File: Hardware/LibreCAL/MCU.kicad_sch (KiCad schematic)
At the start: 30 parts, among them J5 USB_C_Receptacle_USB2.0, J6 TC2030-ARM, SW1 TL3301CF160QG, U5 W25Q16JVSNIQ, U6 IP4234CZ6, U7 RP2040, U8 W25Q16JVSNIQ, Y1 ECS-120-8-36-CKM-TR3

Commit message: Partial routing
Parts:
- removed Y1: ECS-120-8-36-CKM-TR3, Crystal:Crystal_SMD_2520-4Pin_2.5x2.0mm, symbol Device:Crystal_GND2
- added Y1: ECS-120-8-36-CKM-TR3, Crystal:Crystal_SMD_2520-4Pin_2.5x2.0mm, symbol Device:Crystal_GND24
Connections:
- net ADC_TEMP: now also U7.41 (GPIO29_ADC3); no longer U7.38 (GPIO26_ADC0)
- net BUTTON1: now also U7.6 (GPIO4); no longer U7.40 (GPIO28_ADC2)
- net GND: now also Y1.2, Y1.4
- net HEATER: now also U7.40 (GPIO28_ADC2); no longer U7.41 (GPIO29_ADC3)
- net LED_LOAD: now also U7.37 (GPIO25); no longer U7.31 (GPIO20)
- net LED_OPEN: now also U7.35 (GPIO23); no longer U7.29 (GPIO18)
- net LED_PORT1: now also U7.32 (GPIO21); no longer U7.34 (GPIO22)
- net LED_PORT2: now also U7.9 (GPIO7); no longer U7.35 (GPIO23)
- net LED_PORT3: now also U7.34 (GPIO22); no longer U7.36 (GPIO24)
- net LED_PORT4: now also U7.11 (GPIO8); no longer U7.37 (GPIO25)
- net LED_READY: now also U7.7 (GPIO5); no longer U7.27 (GPIO16)
- net LED_SHORT: now also U7.36 (GPIO24); no longer U7.30 (GPIO19)
- net LED_THROUGH: now also U7.38 (GPIO26_ADC0); no longer U7.32 (GPIO21)
- net LED_WAIT: now also U7.8 (GPIO6); no longer U7.28 (GPIO17)
- net P1_V1: now also U7.29 (GPIO18); no longer U7.6 (GPIO4)
- net P1_V2: now also U7.30 (GPIO19); no longer U7.7 (GPIO5)
- net P1_V3: now also U7.31 (GPIO20); no longer U7.8 (GPIO6)
- net P2_V1: now also U7.28 (GPIO17); no longer U7.9 (GPIO7)
- net P2_V2: now also U7.27 (GPIO16); no longer U7.11 (GPIO8)
- net P2_V3: now also U7.18 (GPIO15); no longer U7.12 (GPIO9)
- net P3_V1: now also U7.14 (GPIO11); no longer U7.13 (GPIO10)
- net P3_V2: now also U7.13 (GPIO10); no longer U7.14 (GPIO11)
- net P3_V3: now also U7.12 (GPIO9); no longer U7.15 (GPIO12)
- net P4_V1: now also U7.15 (GPIO12); no longer U7.16 (GPIO13)
- net P4_V2: now also U7.16 (GPIO13); no longer U7.17 (GPIO14)
- net P4_V3: now also U7.17 (GPIO14); no longer U7.18 (GPIO15)
- net at C12.1, U7.20 (XIN): now also Y1.1
- net at J5.A7 (D-), J5.B7 (D-): now also U6.6 (I/O2A); no longer U6.1 (I/O1A)
- net at U6.3 (I/O1B): now also U7.47 (USB_DP); no longer U7.46 (USB_DM)
- net at U6.4 (I/O2B): now also U7.46 (USB_DM); no longer U7.47 (USB_DP)
- net at J5.A6 (D+), J5.B6 (D+): now also U6.1 (I/O1A); no longer U6.6 (I/O2A)
- net at C13.1, U7.21 (XOUT): now also Y1.3
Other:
- moved on the sheet: U6

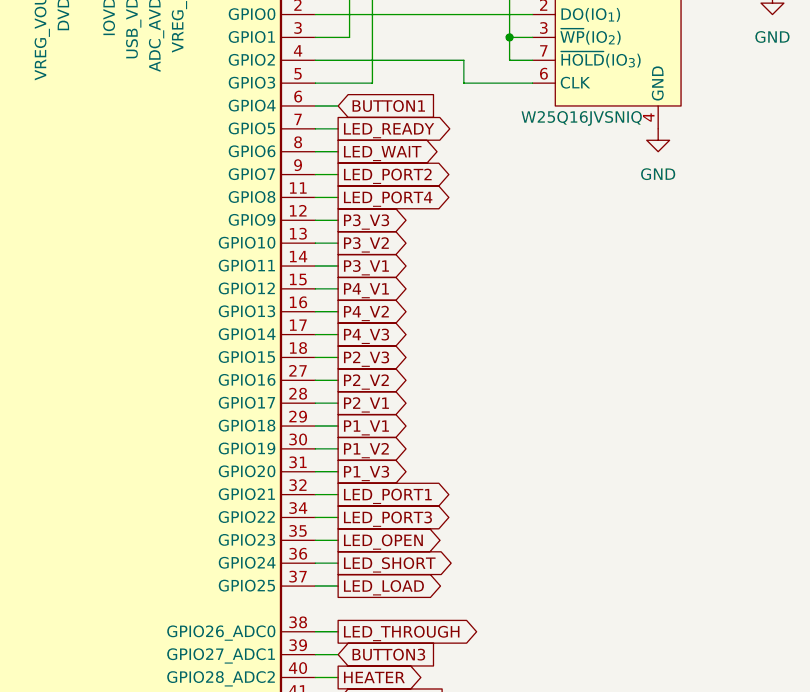
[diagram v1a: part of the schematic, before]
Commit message: Filters added, housing updated
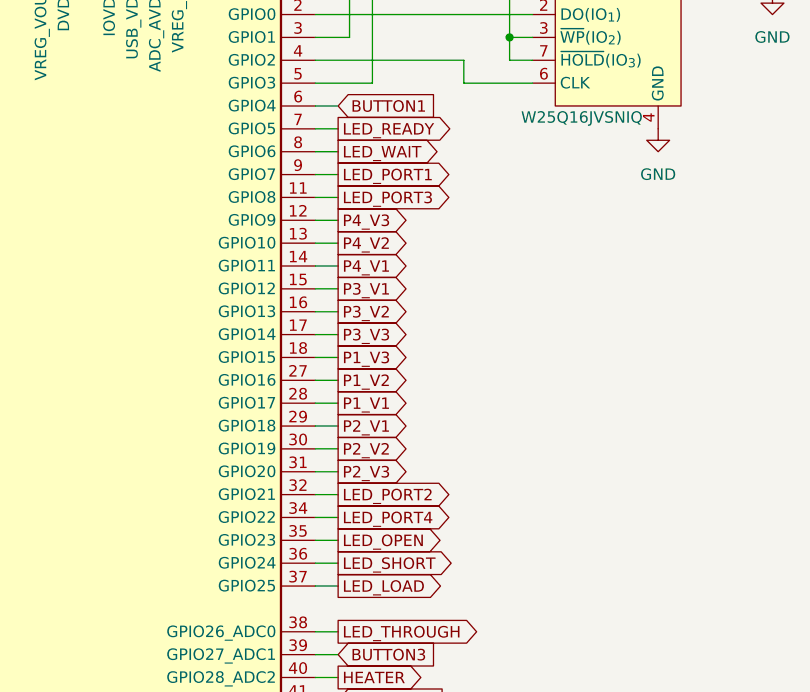
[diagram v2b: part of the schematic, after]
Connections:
- net LED_PORT1: now also U7.9 (GPIO7); no longer U7.32 (GPIO21)
- net LED_PORT2: now also U7.32 (GPIO21); no longer U7.9 (GPIO7)
- net LED_PORT3: now also U7.11 (GPIO8); no longer U7.34 (GPIO22)
- net LED_PORT4: now also U7.34 (GPIO22); no longer U7.11 (GPIO8)
- net P1_V1: now also U7.28 (GPIO17); no longer U7.29 (GPIO18)
- net P1_V2: now also U7.27 (GPIO16); no longer U7.30 (GPIO19)
- net P1_V3: now also U7.18 (GPIO15); no longer U7.31 (GPIO20)
- net P2_V1: now also U7.29 (GPIO18); no longer U7.28 (GPIO17)
- net P2_V2: now also U7.30 (GPIO19); no longer U7.27 (GPIO16)
- net P2_V3: now also U7.31 (GPIO20); no longer U7.18 (GPIO15)
- net P3_V1: now also U7.15 (GPIO12); no longer U7.14 (GPIO11)
- net P3_V2: now also U7.16 (GPIO13); no longer U7.13 (GPIO10)
- net P3_V3: now also U7.17 (GPIO14); no longer U7.12 (GPIO9)
- net P4_V1: now also U7.14 (GPIO11); no longer U7.15 (GPIO12)
- net P4_V2: now also U7.13 (GPIO10); no longer U7.16 (GPIO13)
- net P4_V3: now also U7.12 (GPIO9); no longer U7.17 (GPIO14)
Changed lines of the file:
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@@
     )
   )
-  (global_label "P4_V3" (shape output) (at 204.47 107.95 0) (fields_autoplaced)
+  (global_label "P3_V3" (shape output) (at 204.47 107.95 0) (fields_autoplaced)
     (effects (font (size 1.27 1.27)) (justify left))
     (property "Intersheet References" "${INTERSHEET_REFS}" (id 0) (at 212.6283 107.8706 0)
@@
     )
   )
-  (global_label "P3_V1" (shape output) (at 204.47 100.33 0) (fields_autoplaced)
+  (global_label "P4_V1" (shape output) (at 204.47 100.33 0) (fields_autoplaced)
     (effects (font (size 1.27 1.27)) (justify left))
     (property "Intersheet References" "${INTERSHEET_REFS}" (id 0) (at 212.6283 100.2506 0)
@@
     )
   )
-  (global_label "P1_V3" (shape output) (at 204.47 123.19 0) (fields_autoplaced)
+  (global_label "P2_V3" (shape output) (at 204.47 123.19 0) (fields_autoplaced)
     (effects (font (size 1.27 1.27)) (justify left))
     (property "Intersheet References" "${INTERSHEET_REFS}" (id 0) (at 212.6283 123.1106 0)
@@
     )
   )
-  (global_label "LED_PORT4" (shape output) (at 204.47 92.71 0) (fields_autoplaced)
+  (global_label "LED_PORT3" (shape output) (at 204.47 92.71 0) (fields_autoplaced)
     (effects (font (size 1.27 1.27)) (justify left))
     (property "Intersheet References" "${INTERSHEET_REFS}" (id 0) (at 217.3455 92.6306 0)
@@
     )
   )
-  (global_label "P1_V1" (shape output) (at 204.47 118.11 0) (fields_autoplaced)
+  (global_label "P2_V1" (shape output) (at 204.47 118.11 0) (fields_autoplaced)
     (effects (font (size 1.27 1.27)) (justify left))
     (property "Intersheet References" "${INTERSHEET_REFS}" (id 0) (at 212.6283 118.0306 0)
@@
     )
   )
-  (global_label "P3_V2" (shape output) (at 204.47 97.79 0) (fields_autoplaced)
+  (global_label "P4_V2" (shape output) (at 204.47 97.79 0) (fields_autoplaced)
     (effects (font (size 1.27 1.27)) (justify left))
     (property "Intersheet References" "${INTERSHEET_REFS}" (id 0) (at 212.6283 97.7106 0)
@@
     )
   )
-  (global_label "LED_PORT1" (shape output) (at 204.47 125.73 0) (fields_autoplaced)
+  (global_label "LED_PORT2" (shape output) (at 204.47 125.73 0) (fields_autoplaced)
     (effects (font (size 1.27 1.27)) (justify left))
     (property "Intersheet References" "${INTERSHEET_REFS}" (id 0) (at 217.3455 125.6506 0)
@@
     )
   )
-  (global_label "P2_V1" (shape output) (at 204.47 115.57 0) (fields_autoplaced)
+  (global_label "P1_V1" (shape output) (at 204.47 115.57 0) (fields_autoplaced)
     (effects (font (size 1.27 1.27)) (justify left))
     (property "Intersheet References" "${INTERSHEET_REFS}" (id 0) (at 212.6283 115.4906 0)
@@
     )
   )
-  (global_label "P2_V2" (shape output) (at 204.47 113.03 0) (fields_autoplaced)
+  (global_label "P1_V2" (shape output) (at 204.47 113.03 0) (fields_autoplaced)
     (effects (font (size 1.27 1.27)) (justify left))
     (property "Intersheet References" "${INTERSHEET_REFS}" (id 0) (at 212.6283 112.9506 0)
@@
     )
   )
-  (global_label "P4_V2" (shape output) (at 204.47 105.41 0) (fields_autoplaced)
+  (global_label "P3_V2" (shape output) (at 204.47 105.41 0) (fields_autoplaced)
     (effects (font (size 1.27 1.27)) (justify left))
     (property "Intersheet References" "${INTERSHEET_REFS}" (id 0) (at 212.6283 105.3306 0)
@@
     )
   )
-  (global_label "P4_V1" (shape output) (at 204.47 102.87 0) (fields_autoplaced)
+  (global_label "P3_V1" (shape output) (at 204.47 102.87 0) (fields_autoplaced)
     (effects (font (size 1.27 1.27)) (justify left))
     (property "Intersheet References" "${INTERSHEET_REFS}" (id 0) (at 212.6283 102.7906 0)
@@
     )
   )
-  (global_label "LED_PORT3" (shape output) (at 204.47 128.27 0) (fields_autoplaced)
+  (global_label "LED_PORT4" (shape output) (at 204.47 128.27 0) (fields_autoplaced)
     (effects (font (size 1.27 1.27)) (justify left))
     (property "Intersheet References" "${INTERSHEET_REFS}" (id 0) (at 217.3455 128.1906 0)
@@
     )
   )
-  (global_label "P2_V3" (shape output) (at 204.47 110.49 0) (fields_autoplaced)
+  (global_label "P1_V3" (shape output) (at 204.47 110.49 0) (fields_autoplaced)
     (effects (font (size 1.27 1.27)) (justify left))
     (property "Intersheet References" "${INTERSHEET_REFS}" (id 0) (at 212.6283 110.4106 0)
@@
     )
   )
-  (global_label "P3_V3" (shape output) (at 204.47 95.25 0) (fields_autoplaced)
+  (global_label "P4_V3" (shape output) (at 204.47 95.25 0) (fields_autoplaced)
     (effects (font (size 1.27 1.27)) (justify left))
     (property "Intersheet References" "${INTERSHEET_REFS}" (id 0) (at 212.6283 95.1706 0)
@@
     )
   )
-  (global_label "LED_PORT2" (shape output) (at 204.47 90.17 0) (fields_autoplaced)
+  (global_label "LED_PORT1" (shape output) (at 204.47 90.17 0) (fields_autoplaced)
     (effects (font (size 1.27 1.27)) (justify left))
     (property "Intersheet References" "${INTERSHEET_REFS}" (id 0) (at 217.3455 90.0906 0)
@@
     )
   )
-  (global_label "P1_V2" (shape output) (at 204.47 120.65 0) (fields_autoplaced)
+  (global_label "P2_V2" (shape output) (at 204.47 120.65 0) (fields_autoplaced)
     (effects (font (size 1.27 1.27)) (justify left))
     (property "Intersheet References" "${INTERSHEET_REFS}" (id 0) (at 212.6283 120.5706 0)

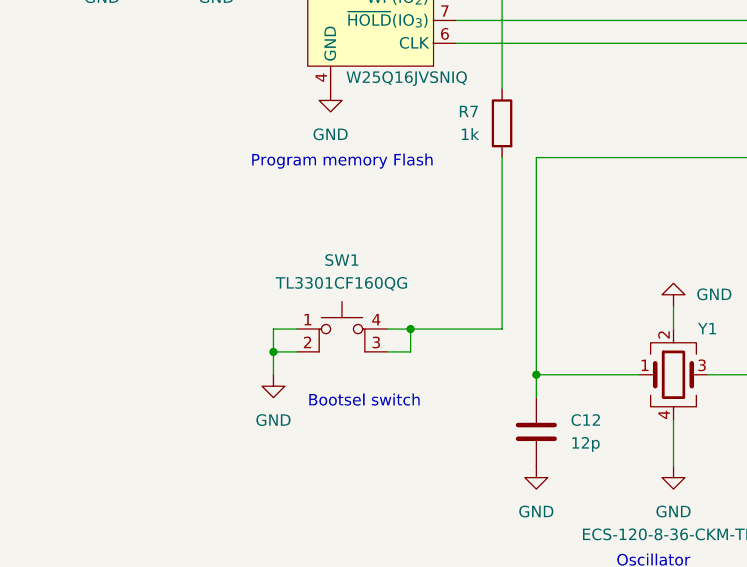
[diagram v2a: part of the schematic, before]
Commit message: replaced bootsel switch, adjusted covers
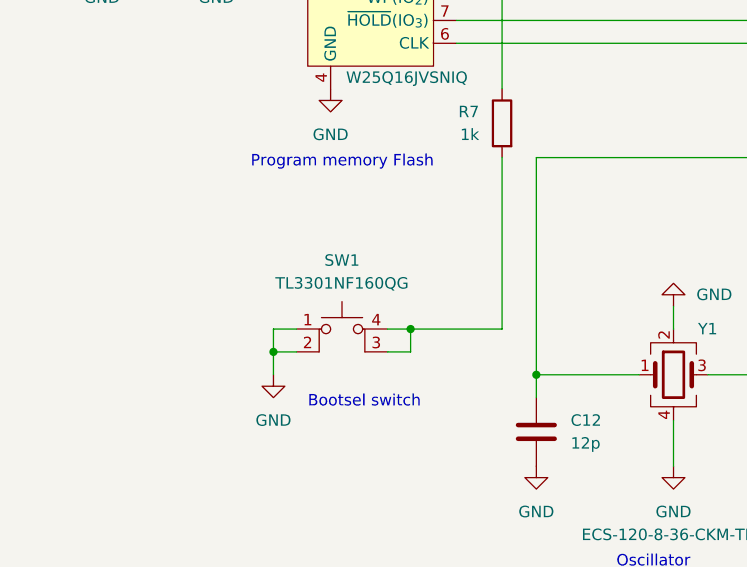
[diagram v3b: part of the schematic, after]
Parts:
- SW1: value TL3301CF160QG -> TL3301NF160QG; footprint LibreCAL:TL3301-J -> LibreCAL:TL3301N-J
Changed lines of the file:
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@@
     (in_bom yes) (on_board yes) (fields_autoplaced)
     (property "Reference" "SW1" (id 0) (at 57.15 129.54 0))
-    (property "Value" "TL3301CF160QG" (id 1) (at 57.15 132.08 0))
-    (property "Footprint" "LibreCAL:TL3301-J" (id 2) (at 57.15 132.08 0)
+    (property "Value" "TL3301NF160QG" (id 1) (at 57.15 132.08 0))
+    (property "Footprint" "LibreCAL:TL3301N-J" (id 2) (at 57.15 132.08 0)
       (effects (font (size 1.27 1.27)) hide)
     )

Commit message: Improvements on LibreCAL KiCad: fixed minor errors/labels(cosmetic), improved BOM(Added LCSC_Part), improved Impedance JLCPCB 4Layer JLC7628 1.6mm
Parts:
- C10, C21, C23, C24, C25: LCSC_Part (none) -> C307418
- C11, C14, C15, C16, C17, C18, C19, C20, C22, C26, C9: LCSC_Part (none) -> C307331
- C12, C13: LCSC_Part (none) -> C76948
- FB1: LCSC_Part (none) -> C404693
- J5: LCSC_Part (none) -> C165948
- J6: LCSC_Part (none) -> NA
- R5, R6: LCSC_Part (none) -> C105872
- R7: LCSC_Part (none) -> C106235
- SW1: LCSC_Part (none) -> C273527
- U5, U8: LCSC_Part (none) -> C115407
- U6: LCSC_Part (none) -> C455086
- U7: LCSC_Part (none) -> C2040
- Y1: LCSC_Part (none) -> C5349079
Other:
- title: (none) -> LibreCAL
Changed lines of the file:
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@@
 (kicad_sch (version 20211123) (generator eeschema)
   (paper "A4")
+  (title_block
+    (title "LibreCAL")
+    (date "2023-01-07")
+    (rev "A+")
+  )
   (junction (at 91.44 30.48) (diameter 0) (color 0 0 0 0)
   )
@@
       (effects (font (size 1.27 1.27)) hide)
     )
+    (property "LCSC_Part" "C76948" (id 4) (at 78.74 148.59 0)
+      (effects (font (size 1.27 1.27)) hide)
+    )
     (pin "1")
     (pin "2")
@@
       (effects (font (size 1.27 1.27)) hide)
     )
+    (property "LCSC_Part" "C307331" (id 4) (at 265.43 66.04 0)
+      (effects (font (size 1.27 1.27)) hide)
+    )
     (pin "1")
     (pin "2")
@@
       (effects (font (size 1.27 1.27)) hide)
     )
+    (property "LCSC_Part" "C307331" (id 4) (at 30.48 91.44 0)
+      (effects (font (size 1.27 1.27)) hide)
+    )
     (pin "1")
     (pin "2")
@@
     )
     (property "Datasheet" "https://assets.nexperia.com/documents/data-sheet/IP4234CZ6.pdf" (id 3) (at 91.44 49.53 0)
+      (effects (font (size 1.27 1.27)) hide)
+    )
+    (property "LCSC_Part" "C455086" (id 4) (at 91.44 49.53 0)
       (effects (font (size 1.27 1.27)) hide)
     )
@@
       (effects (font (size 1.27 1.27)) hide)
     )
+    (property "LCSC_Part" "C5349079" (id 4) (at 93.98 142.24 0)
+      (effects (font (size 1.27 1.27)) hide)
+    )
     (pin "1")
     (pin "2")
@@
       (effects (font (size 1.27 1.27)) hide)
     )
+    (property "LCSC_Part" "C307418" (id 4) (at 194.31 57.15 0)
+      (effects (font (size 1.27 1.27)) hide)
+    )
     (pin "1")
     (pin "2")
@@
     )
     (property "Datasheet" "~" (id 3) (at 64.77 67.31 0)
+      (effects (font (size 1.27 1.27)) hide)
+    )
+    (property "LCSC_Part" "C105872" (id 4) (at 64.77 67.31 0)
       (effects (font (size 1.27 1.27)) hide)
     )
@@
       (effects (font (size 1.27 1.27)) hide)
     )
+    (property "LCSC_Part" "C273527" (id 4) (at 57.15 139.7 0)
+      (effects (font (size 1.27 1.27)) hide)
+    )
     (pin "1")
     (pin "2")
@@
       (effects (font (size 1.27 1.27)) hide)
     )
+    (property "LCSC_Part" "C307331" (id 4) (at 110.49 31.75 0)
+      (effects (font (size 1.27 1.27)) hide)
+    )
     (pin "1")
     (pin "2")
@@
       (effects (font (size 1.27 1.27)) hide)
     )
+    (property "LCSC_Part" "C76948" (id 4) (at 109.22 148.59 0)
+      (effects (font (size 1.27 1.27)) hide)
+    )
     (pin "1")
     (pin "2")
@@
     )
     (property "Datasheet" "~" (id 3) (at 167.64 31.75 0)
+      (effects (font (size 1.27 1.27)) hide)
+    )
+    (property "LCSC_Part" "C307331" (id 4) (at 167.64 31.75 0)
       (effects (font (size 1.27 1.27)) hide)
     )
@@
     )
     (property "Datasheet" "https://www.usb.org/sites/default/files/documents/usb_type-c.zip" (id 3) (at 39.37 45.72 0)
+      (effects (font (size 1.27 1.27)) hide)
+    )
+    (property "LCSC_Part" "C165948" (id 4) (at 35.56 45.72 0)
       (effects (font (size 1.27 1.27)) hide)
     )
@@
       (effects (font (size 1.27 1.27)) hide)
     )
+    (property "LCSC_Part" "C307418" (id 4) (at 162.56 57.15 0)
+      (effects (font (size 1.27 1.27)) hide)
+    )
     (pin "1")
     (pin "2")
@@
     )
     (property "Datasheet" "~" (id 3) (at 133.35 31.75 0)
+      (effects (font (size 1.27 1.27)) hide)
+    )
+    (property "LCSC_Part" "C307331" (id 4) (at 133.35 31.75 0)
       (effects (font (size 1.27 1.27)) hide)
     )
@@
       (effects (font (size 1.27 1.27)) hide)
     )
+    (property "LCSC_Part" "C307418" (id 4) (at 198.12 31.75 0)
+      (effects (font (size 1.27 1.27)) hide)
+    )
     (pin "1")
     (pin "2")
@@
     )
     (property "Datasheet" "~" (id 3) (at 149.86 57.15 0)
+      (effects (font (size 1.27 1.27)) hide)
+    )
+    (property "LCSC_Part" "C307331" (id 4) (at 149.86 57.15 0)
       (effects (font (size 1.27 1.27)) hide)
     )
@@
       (effects (font (size 1.27 1.27)) hide)
     )
+    (property "LCSC_Part" "C307418" (id 4) (at 43.18 91.44 0)
+      (effects (font (size 1.27 1.27)) hide)
+    )
     (pin "1")
     (pin "2")
@@
     )
     (property "Datasheet" "~" (id 3) (at 138.43 57.15 0)
+      (effects (font (size 1.27 1.27)) hide)
+    )
+    (property "LCSC_Part" "C307331" (id 4) (at 138.43 57.15 0)
       (effects (font (size 1.27 1.27)) hide)
     )
@@
       (effects (font (size 1.27 1.27)) hide)
     )
+    (property "LCSC_Part" "C307331" (id 4) (at 144.78 31.75 0)
+      (effects (font (size 1.27 1.27)) hide)
+    )
     (pin "1")
     (pin "2")
@@
       (effects (font (size 1.27 1.27)) hide)
     )
+    (property "LCSC_Part" "C307418" (id 4) (at 252.73 66.04 0)
+      (effects (font (size 1.27 1.27)) hide)
+    )
     (pin "1")
     (pin "2")
@@
     )
     (property "Datasheet" "https://datasheets.raspberrypi.com/rp2040/rp2040-datasheet.pdf" (id 3) (at 176.53 110.49 0)
+      (effects (font (size 1.27 1.27)) hide)
+    )
+    (property "LCSC_Part" "C2040" (id 4) (at 176.53 110.49 0)
       (effects (font (size 1.27 1.27)) hide)
     )
@@
       (effects (font (size 1.27 1.27)) hide)
     )
+    (property "LCSC_Part" "C105872" (id 4) (at 55.88 67.31 0)
+      (effects (font (size 1.27 1.27)) hide)
+    )
     (pin "1")
     (pin "2")
@@
       (effects (font (size 1.27 1.27)) hide)
     )
+    (property "LCSC_Part" "C307331" (id 4) (at 76.2 35.56 0)
+      (effects (font (size 1.27 1.27)) hide)
+    )
     (pin "1")
     (pin "2")
@@
     )
     (property "Datasheet" "~" (id 3) (at 156.21 31.75 0)
+      (effects (font (size 1.27 1.27)) hide)
+    )
+    (property "LCSC_Part" "C307331" (id 4) (at 156.21 31.75 0)
       (effects (font (size 1.27 1.27)) hide)
     )
@@
       (effects (font (size 1.27 1.27)) hide)
     )
+    (property "LCSC_Part" "C404693" (id 4) (at 184.15 25.4 0)
+      (effects (font (size 1.27 1.27)) hide)
+    )
     (pin "1")
     (pin "2")
@@
     )
     (property "Datasheet" "~" (id 3) (at 121.92 31.75 0)
+      (effects (font (size 1.27 1.27)) hide)
+    )
+    (property "LCSC_Part" "C307331" (id 4) (at 121.92 31.75 0)
       (effects (font (size 1.27 1.27)) hide)
     )
@@
     )
     (property "Datasheet" "https://www.winbond.com/hq/support/documentation/levelOne.jsp?__locale=en&DocNo=DA00-W25Q16JV.1" (id 3) (at 58.42 97.79 0)
+      (effects (font (size 1.27 1.27)) hide)
+    )
+    (property "LCSC_Part" "C115407" (id 4) (at 58.42 97.79 0)
       (effects (font (size 1.27 1.27)) hide)
     )
@@
       (effects (font (size 1.27 1.27)) hide)
     )
+    (property "LCSC_Part" "C115407" (id 4) (at 237.49 72.39 0)
+      (effects (font (size 1.27 1.27)) hide)
+    )
     (pin "1")
     (pin "2")
@@
       (effects (font (size 1.27 1.27)) hide)
     )
+    (property "LCSC_Part" "NA" (id 4) (at 129.54 153.67 0)
+      (effects (font (size 1.27 1.27)) hide)
+    )
     (pin "1")
     (pin "2")
@@
       (effects (font (size 1.27 1.27)) hide)
     )
+    (property "LCSC_Part" "C106235" (id 4) (at 74.93 114.3 0)
+      (effects (font (size 1.27 1.27)) hide)
+    )
